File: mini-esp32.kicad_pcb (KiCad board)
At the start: 4 copper layers, 29 x 58 mm, 47 parts, among them J1 BAT, J2 USB_B_Micro, J5 Conn_01x18, J6 Conn_01x18, Q1 AO3401A, Q2 S8050, Q3 S8050, SW1 RESET, U1 ESP32-WROOM-32E, U2 RT9080-33GJ5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

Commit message: Missing commit
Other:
- board text added: "Mini ESP32 4.0 @serialx"
- board text removed: "Mini ESP32 V3.0.1"
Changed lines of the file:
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@@
     (effects (font (size 0.8 0.8) (thickness 0.15)))
   )
-  (gr_text "Mini ESP32\nV3.0.1" (at 133.4 91 90) (layer B.SilkS)
-    (effects (font (size 4 4) (thickness 0.75)) (justify mirror))
+  (gr_text "Mini ESP32\n4.0 @serialx" (at 134 70.1 90) (layer B.SilkS)
+    (effects (font (size 4 4) (thickness 0.75)) (justify left mirror))
   )
   (gr_text 36 (at 144.526 69.088 90) (layer F.SilkS)

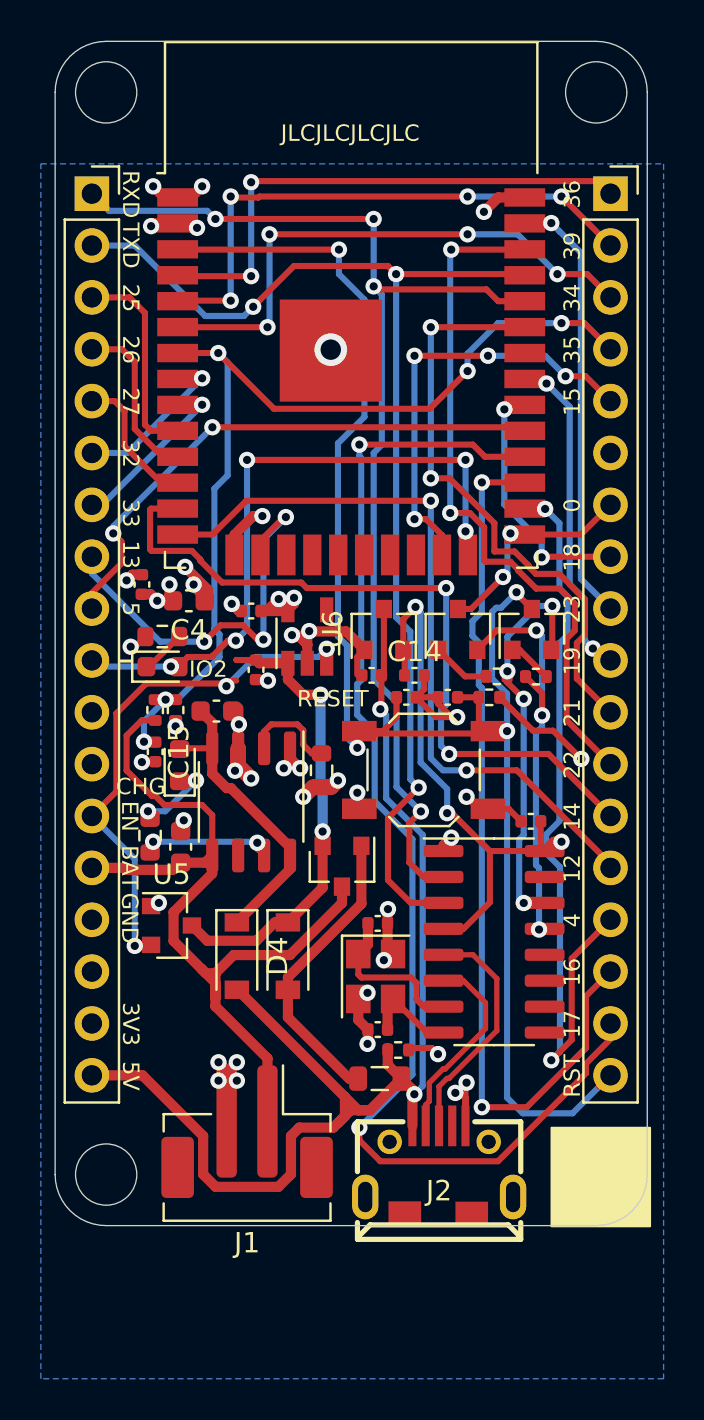
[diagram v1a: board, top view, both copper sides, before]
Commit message: Change USB-to-Serial to CP2104
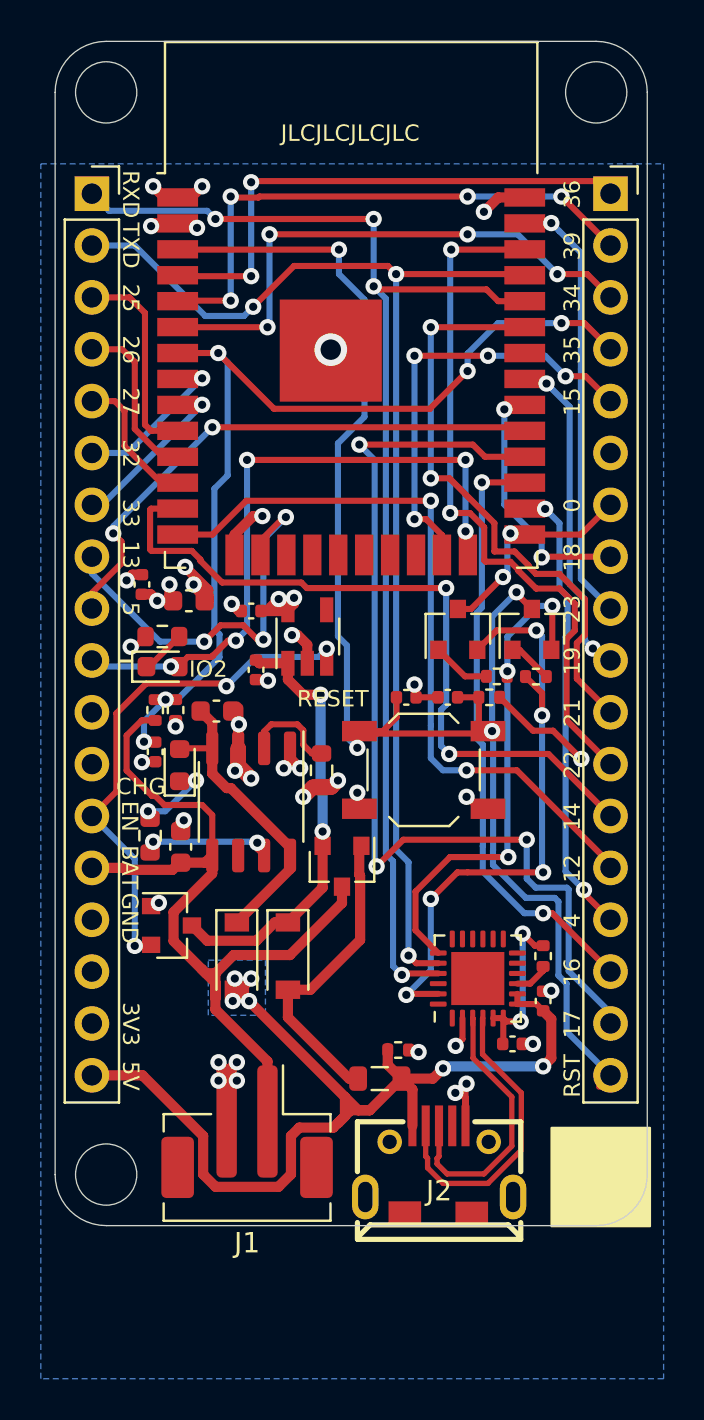
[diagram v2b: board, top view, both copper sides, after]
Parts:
- removed C12: 100n, Capacitor_SMD:C_0402_1005Metric
- removed C13, C14: 1u, Capacitor_SMD:C_0402_1005Metric
- removed U6: XC6206P332MR, Package_TO_SOT_SMD:SOT-23
- removed Y1: 12MHz, Crystal:Crystal_SMD_3225-4Pin_3.2x2.5mm
- added R2: 10k, Resistor_SMD:R_0402_1005Metric, F.Cu at (143.1, 106.4)
- C10: value 22p -> 100n
- C9: value 22p -> 1u
- U4: value CH340G -> CP2104; footprint Package_SO:SOIC-16_3.9x9.9mm_P1.27mm -> Package_DFN_QFN:QFN-24-1EP_4x4mm_P0.5mm_EP2.6x2.6mm
- moved C9 8.95 mm to (143.1, 108.6), turned to 90 degrees
- moved C10 6.64 mm to (141.6, 110.7), turned to 0 degrees
- moved U4 1.97 mm to (139.9, 107.5), turned to 90 degrees
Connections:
- C9 pad 1: Net-(C9-Pad1) -> VBUS
- U4 pad 1: GND -> Net-(U4-Pad1)
- U4 pad 13: DTR -> Net-(U4-Pad13)
- U4 pad 14: RTS -> Net-(U4-Pad14)
- U4 pad 16: CH340_VCC -> Net-(U4-Pad16)
- U4 pad 2: RXD0 -> GND
- U4 pad 3: TXD0 -> UD+
- U4 pad 4: CH340_VCC -> UD-
- U4 pad 5: UD+ -> Net-(C10-Pad1)
- U4 pad 6: UD- -> Net-(C10-Pad1)
- U4 pad 7: Net-(C9-Pad1) -> VBUS
- U4 pad 8: Net-(C10-Pad1) -> VBUS
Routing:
- net CH340_VCC: track 27.8 -> 0.00 mm, vias 3 -> 0
- net GND: track 64.2 -> 47.1 mm, vias 38 -> 35
- net IO16: track 44.9 -> 29.7 mm
- net IO4: track 37.9 -> 23.0 mm
- net IO17: track 61.7 -> 49.5 mm, vias 2 -> 3
- net VBUS: track 61.7 -> 51.0 mm, vias 2 -> 6
- net DTR: track 20.8 -> 30.3 mm, vias 3 -> 5
- net Net-(C9-Pad1): track 7.99 -> 0.00 mm
- net RESET: track 81.0 -> 75.8 mm
- net RTS: track 19.6 -> 24.8 mm, vias 4 -> 3
- net UD-: track 9.80 -> 14.9 mm
- net RXD0: track 57.2 -> 61.4 mm
- net Net-(C10-Pad1): track 4.77 -> 8.28 mm, vias 0 -> 2
- net UD+: track 11.5 -> 13.4 mm
- net Net-(R2-Pad2): track 0.00 -> 1.73 mm
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- added copper zone on B.Cu, net VBUS
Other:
- board text added: "Mini ESP32 4.1 @serialx"
- board text removed: "Mini ESP32 4.0 @serialx"
